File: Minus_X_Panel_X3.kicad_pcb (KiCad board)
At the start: 2 copper layers, 82.9 x 207.4 mm, 11 parts

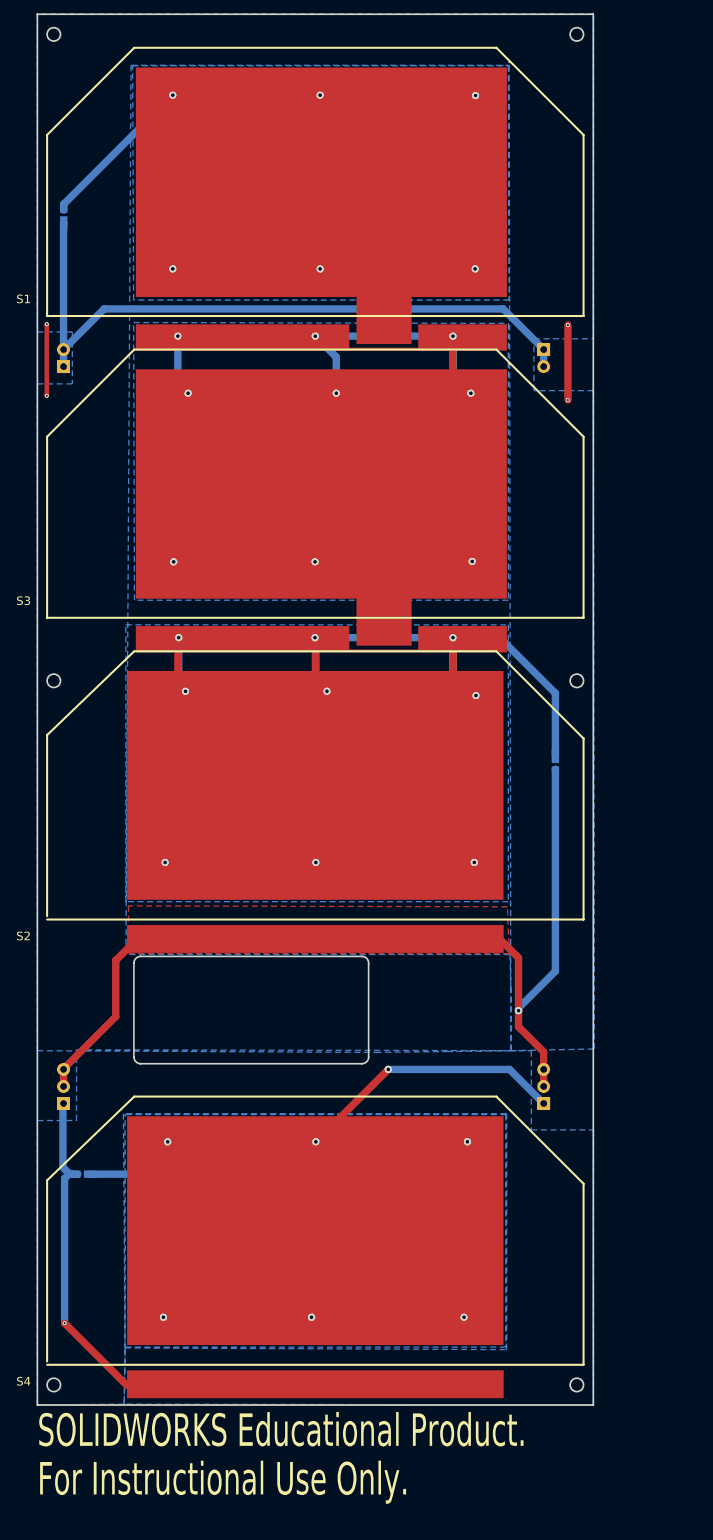
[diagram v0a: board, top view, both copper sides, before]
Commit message: Updated the Pin Configuration
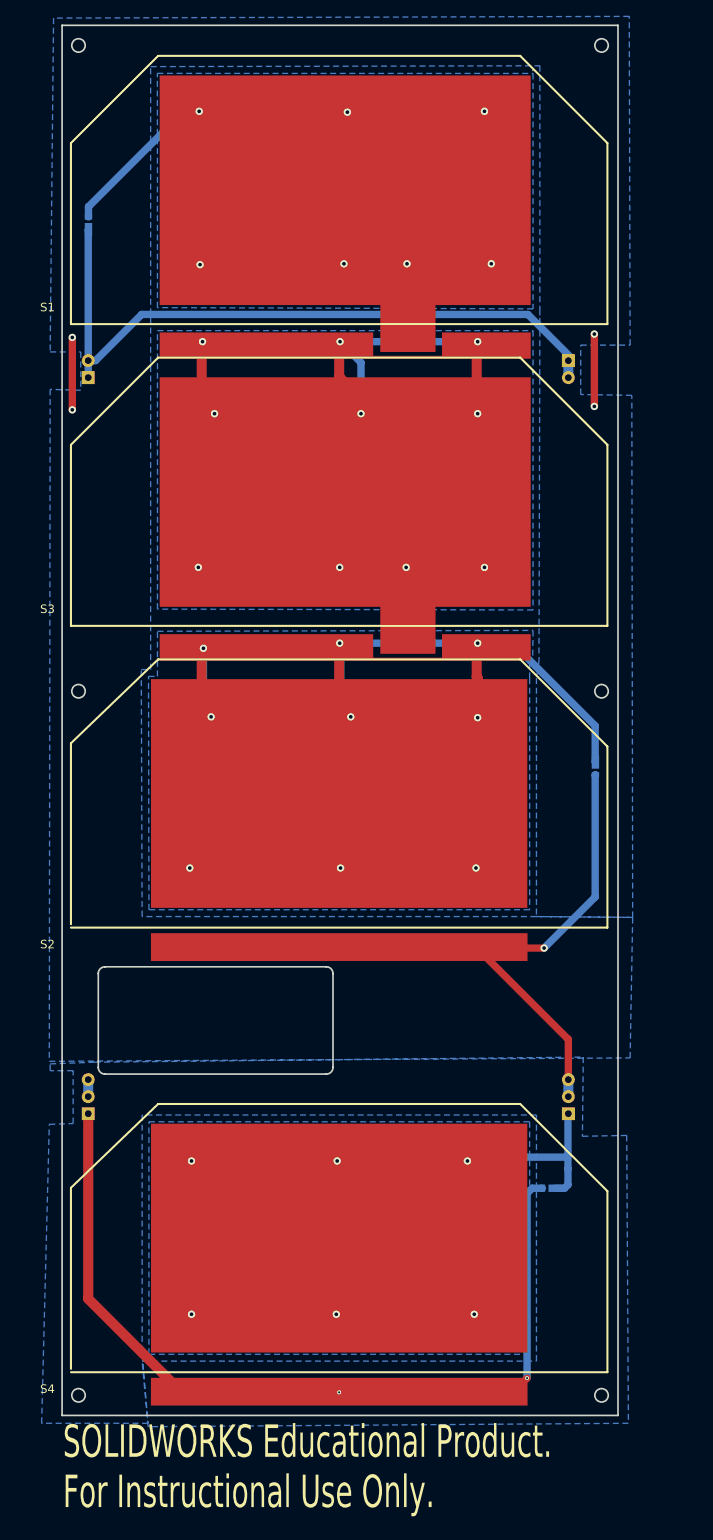
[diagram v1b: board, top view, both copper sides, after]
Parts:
- moved D3 69.3 mm to (232.0, 212.4)
- moved D2 6.03 mm to (238.9, 149.8)
- moved U$1 4.04 mm to (234.9, 89.0)
- moved U$2 4.04 mm to (163.3, 91.5)
- moved U$3 3.98 mm to (234.9, 201.3)
- moved U$4 3.98 mm to (163.3, 201.3)
- moved D1 3.82 mm to (163.3, 68.5)
- moved S1 3.76 mm to (160.7, 83.5)
- moved S2 3.76 mm to (160.7, 173.5)
- moved S3 3.76 mm to (160.7, 128.5)
- moved S4 3.72 mm to (160.7, 239.8)
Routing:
- net /+V3D: track 185.0 -> 135.2 mm, vias 7 -> 6
- net /+V3B: track 204.9 -> 239.0 mm, vias 9 -> 10
- net Net-(D3-A): track 55.9 -> 88.9 mm, vias 1 -> 2
- net GND: track 124.8 -> 112.2 mm
- net /+V3A: track 250.8 -> 253.8 mm
- net /+V3C: track 154.5 -> 157.1 mm, vias 6 -> 7
- net Net-(D1-K): track 100.6 -> 102.1 mm
- removed copper zone on F.Cu, net GND
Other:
- board size 82.9 x 207.4 mm -> 82.9 x 207.3 mm
